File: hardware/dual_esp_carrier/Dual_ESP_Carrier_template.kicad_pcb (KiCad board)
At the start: 2 copper layers, 100 x 100 mm, 40 parts, among them J1 ESP32_lafvin, J2 ESP32_B_LANDSCAPE, J3 SX1278_LORA_2x4, J6 GPS_LC29H_7PIN, SW1 subir ancora, SW2 MODE, SW3 largar ancora, SW4 BOOT

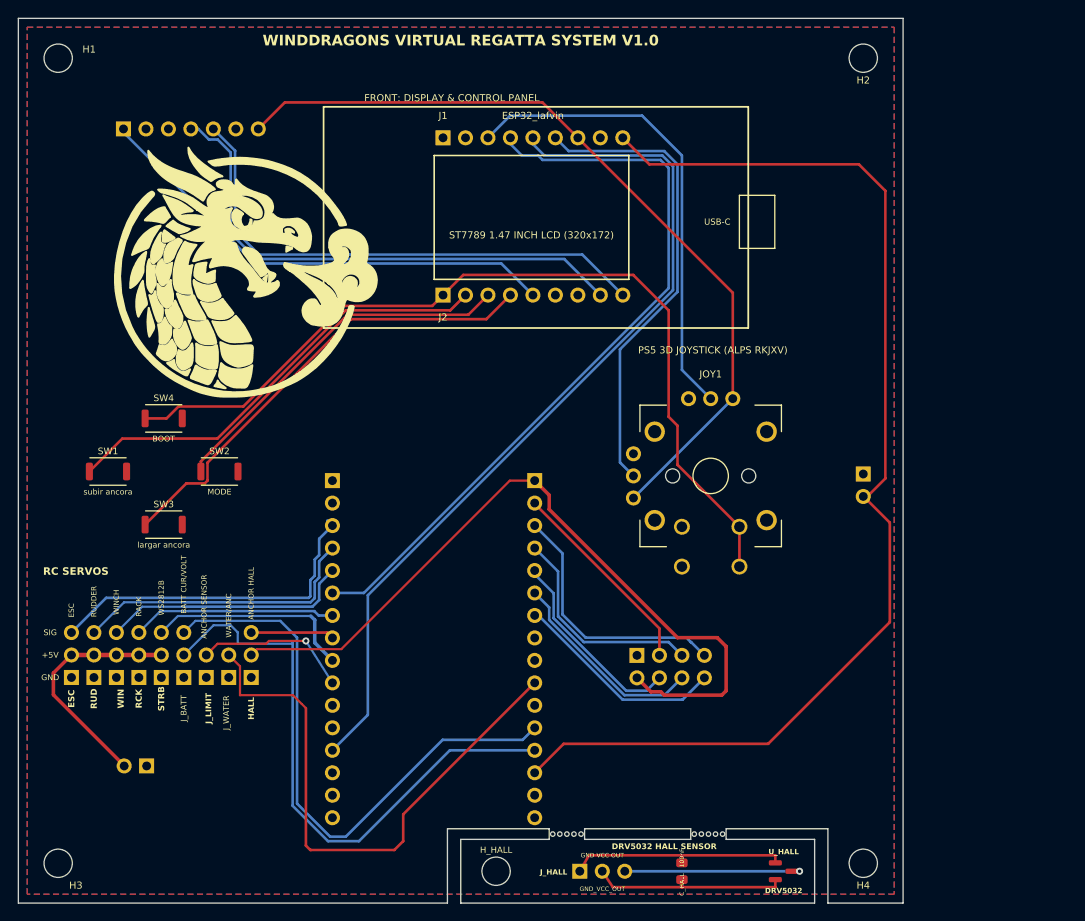
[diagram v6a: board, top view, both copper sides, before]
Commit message: feat: add Dual ESP32-C6 Over-The-Air (OTA) firmware update UI and bundling script
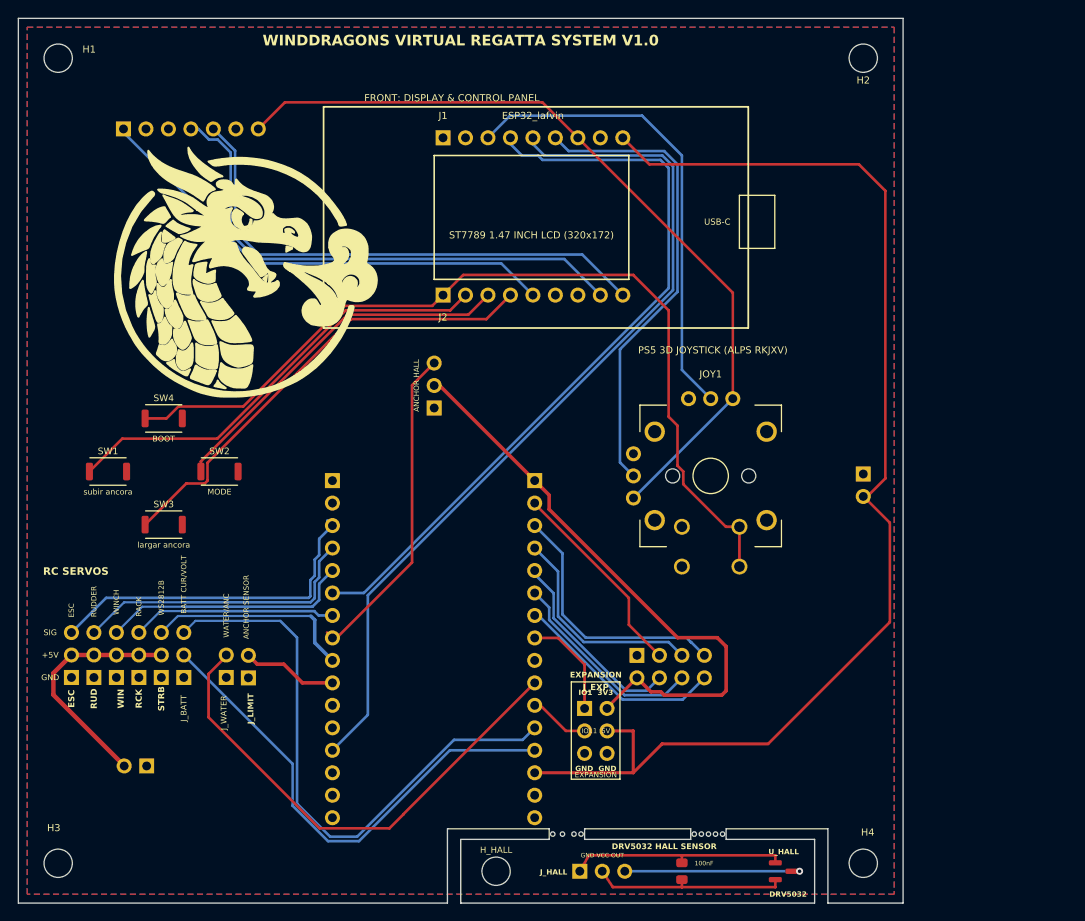
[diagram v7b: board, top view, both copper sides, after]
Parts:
- removed the STAMP at (62.0, 92.2)
- added J_EXP: EXPANSION, Connector_PinHeader_2.54mm:PinHeader_2x03_P2.54mm_Vertical, F.Cu at (64.0, 78.0)
- moved HALL 36.8 mm to (47.0, 44.0)
- moved J_LIMIT 4.76 mm to (26.0, 74.5)
- moved STAMP 0.30 mm to (61.5, 92.2)
- moved J_WATER 0.28 mm to (23.5, 74.5)
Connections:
- J_DK_L pad 11: (no net) -> /EXP_IO11
- J_DK_L pad 8: (no net) -> /EXP_IO1
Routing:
- net /ANCHOR_HALL: track 9.43 -> 37.0 mm
- net /+3V3_C6: track 86.7 -> 67.1 mm
- net /BATT_CURR: track 67.3 -> 55.4 mm
- net /EXP_IO1: track 0.00 -> 11.9 mm
- net /+5V: track 130.7 -> 138.4 mm
- net /WATER_SENS: track 64.3 -> 56.8 mm
- net /EXP_IO11: track 0.00 -> 6.84 mm
- net /ANCHOR_LIMIT: track 17.5 -> 10.8 mm, vias 1 -> 0
- net /IO9_BOOT: track 99.8 -> 100.7 mm
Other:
- board text added: "EXPANSION"
- board text added: "GND GND"
- board text added: "IO1 3V3"
- board text added: "IO11 5V"

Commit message: update PCB layout and regenerate manufacturing gerbers and firmware archives
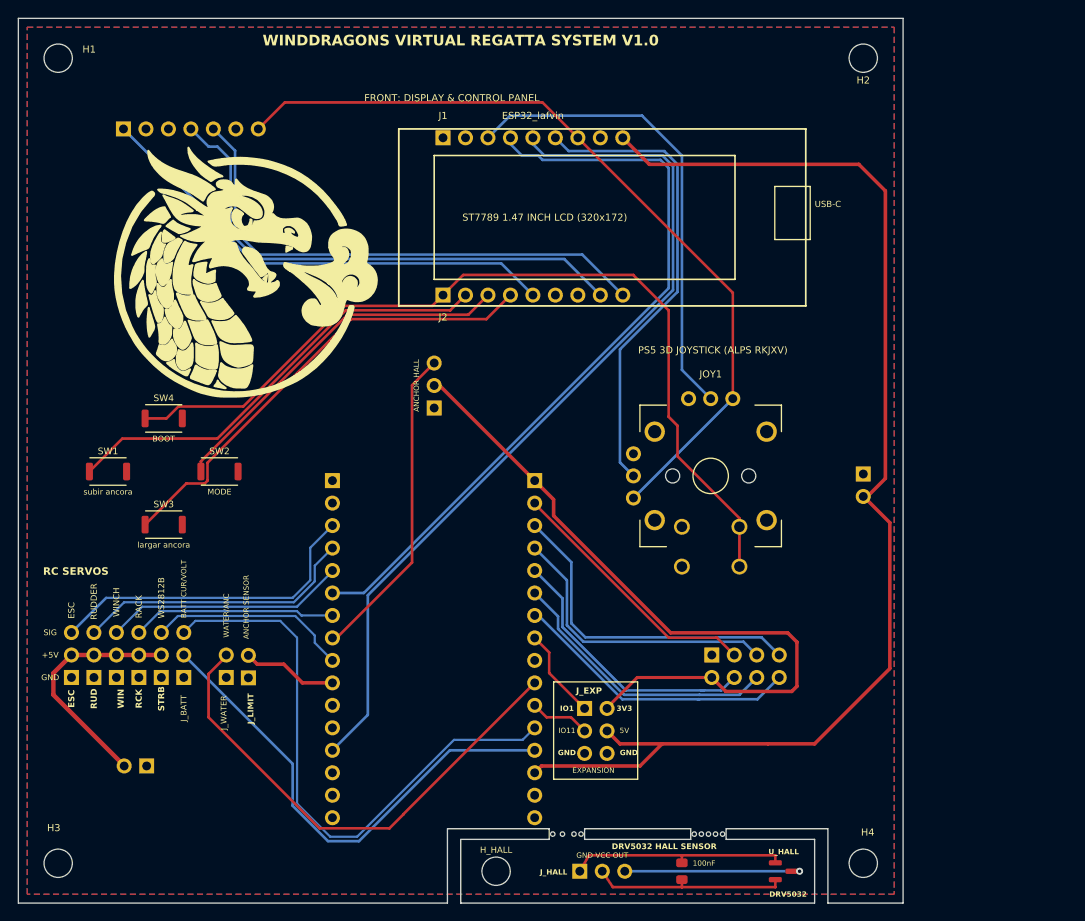
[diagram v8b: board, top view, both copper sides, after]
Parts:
- moved J3 8.46 mm to (86.0, 72.0)
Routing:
- net /+3V3_C6: track 67.1 -> 82.9 mm
- net /LORA_NSS: track 22.2 -> 31.0 mm
- net /LORA_DIO0: track 24.1 -> 32.8 mm
- net /LORA_MOSI: track 23.1 -> 31.5 mm
- net /LORA_MISO: track 29.3 -> 37.8 mm
- net /LORA_SCK: track 24.6 -> 33.1 mm
- net /LORA_RST: track 23.1 -> 29.7 mm
- net /+5V: track 138.4 -> 140.6 mm
- net /SERVO_ESC: track 38.5 -> 36.7 mm
- net /EXP_IO1: track 11.9 -> 10.3 mm
- net /SERVO_RUDDER: track 33.1 -> 32.0 mm
- net /STROBE_DIN: track 23.7 -> 22.7 mm
- net /SERVO_WINCH: track 28.4 -> 27.4 mm
- net /IO9_BOOT: track 100.7 -> 99.8 mm
- net /ANCHOR_HALL: track 37.0 -> 36.1 mm
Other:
- board text added: "3V3"
- board text added: "5V"
- board text added: "IO1"
- board text added: "IO11"
- board text removed: "DIRECT LEDC PWM SERVOS"
- board text removed: "EXPANSION"
- board text removed: "GND GND"
- board text removed: "IO1 3V3"
- board text removed: "IO11 5V"
